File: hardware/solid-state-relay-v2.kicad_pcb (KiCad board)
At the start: 2 copper layers, 40 x 19 mm, 22 parts, among them P1 CON-SENSOR2, P2 TST, P3 TST, P5 BOOT, Q1 2N7002P, U1 XMC110024, U2 DRILL, U3 DRILL

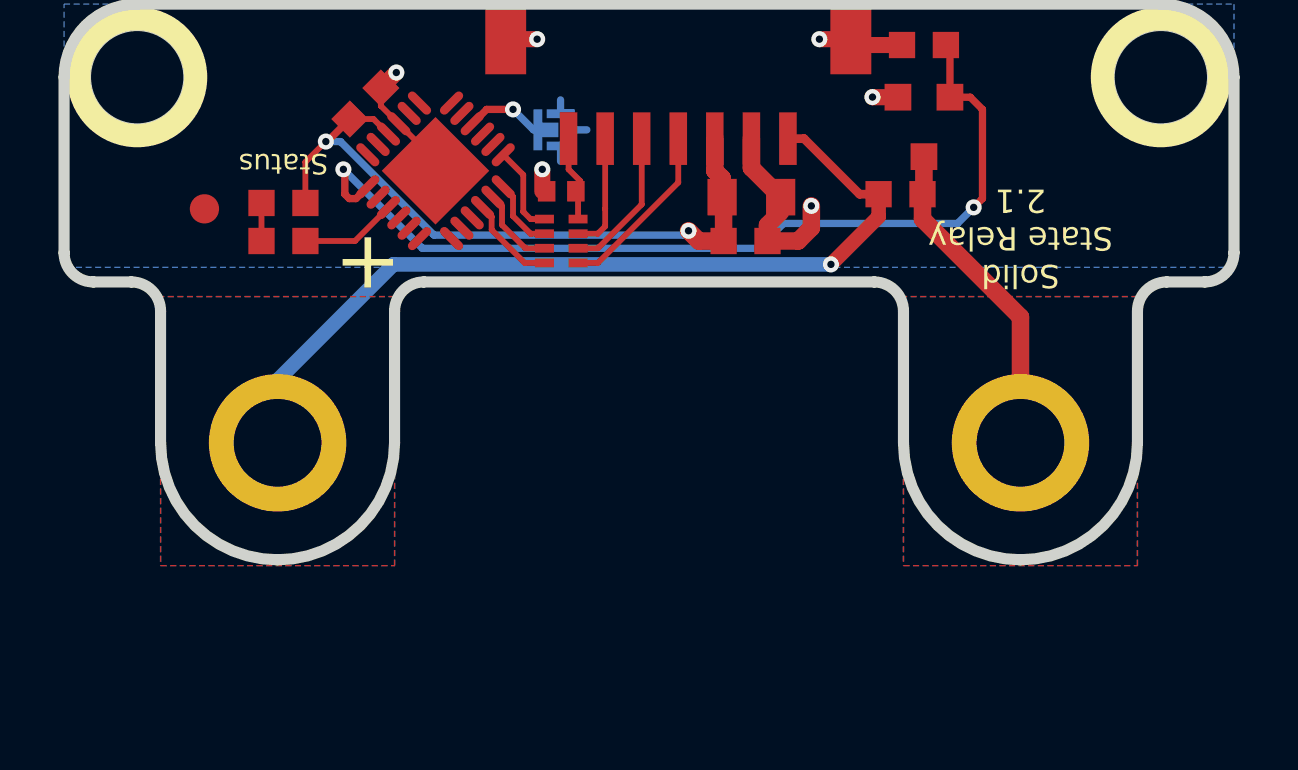
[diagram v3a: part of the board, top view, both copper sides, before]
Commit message: version 2.2: add slotted holes
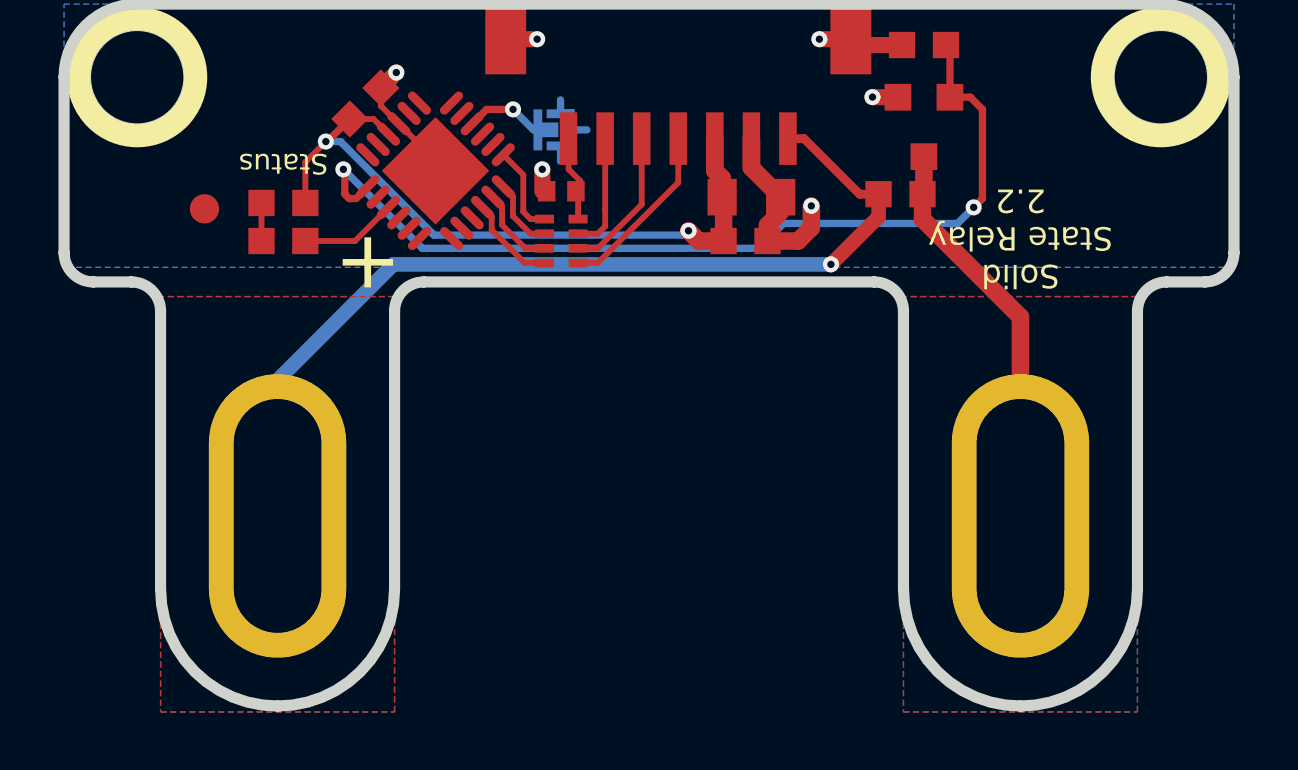
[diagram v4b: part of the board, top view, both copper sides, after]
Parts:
- moved P2 2.50 mm to (137.8, 105.1), turned to 0 degrees
- moved P3 2.50 mm to (163.2, 105.1), turned to 0 degrees
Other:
- board size 40 x 19 mm -> 40 x 24 mm
- board text added: "Copyright Tinkerforge GmbH 2025. This documentation describes Open Hardware and is licensed under the CERN OHL v. 1.1. You may redistribute and modify this documentation under the terms of the CERN OHL v.1.1. (http://ohwr.org/cernohl). This documentation is distributed WITHOUT ANY EXPRESS OR IMPLIED WARRANTY, INCLUDING OF MERCHANTABILITY, SATISFACTORY QUALITY AND FITNESS FOR A PARTICULAR PURPOSE.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"
- board text added: "Solid State Relay 2.2"
- board text removed: "Copyright Tinkerforge GmbH 2023. This documentation describes Open Hardware and is licensed under the CERN OHL v. 1.1. You may redistribute and modify this documentation under the terms of the CERN OHL v.1.1. (http://ohwr.org/cernohl). This documentation is distributed WITHOUT ANY EXPRESS OR IMPLIED WARRANTY, INCLUDING OF MERCHANTABILITY, SATISFACTORY QUALITY AND FITNESS FOR A PARTICULAR PURPOSE.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"
- board text removed: "Solid State Relay 2.1"

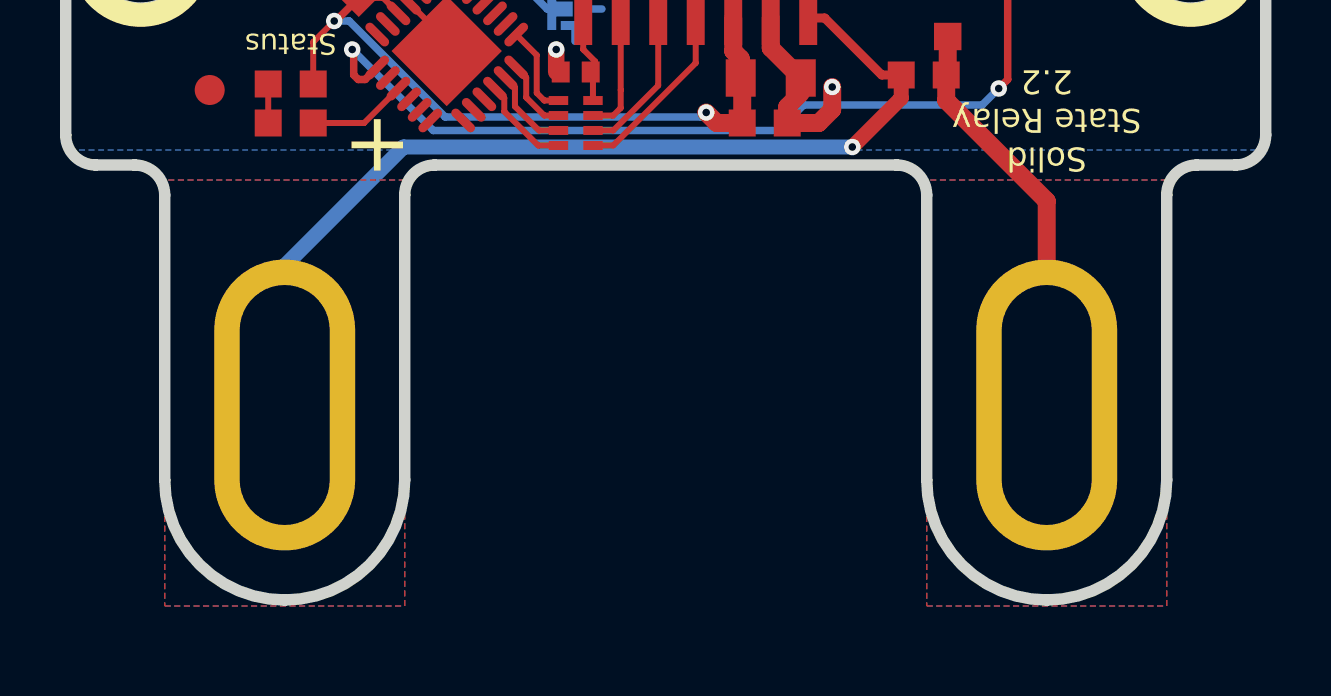
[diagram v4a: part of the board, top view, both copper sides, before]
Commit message: adapt outline to 5mm grid
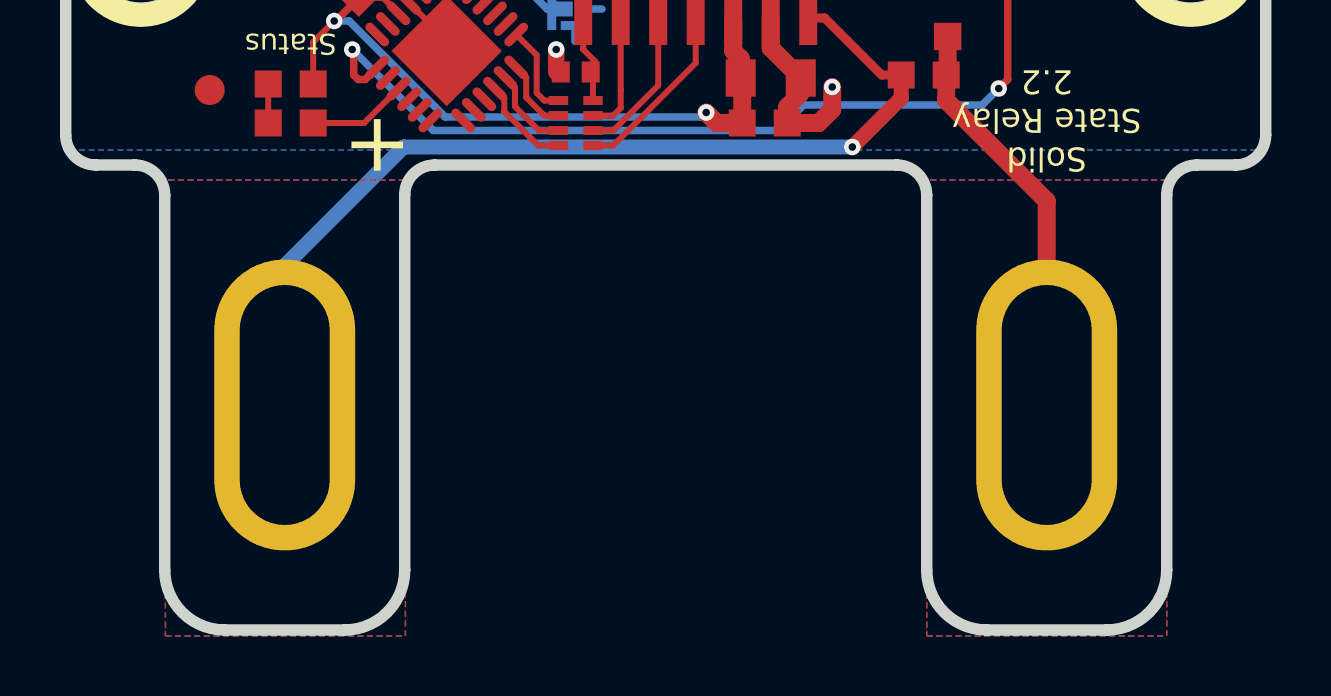
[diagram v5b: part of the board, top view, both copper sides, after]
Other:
- board size 40 x 24 mm -> 40 x 25 mm

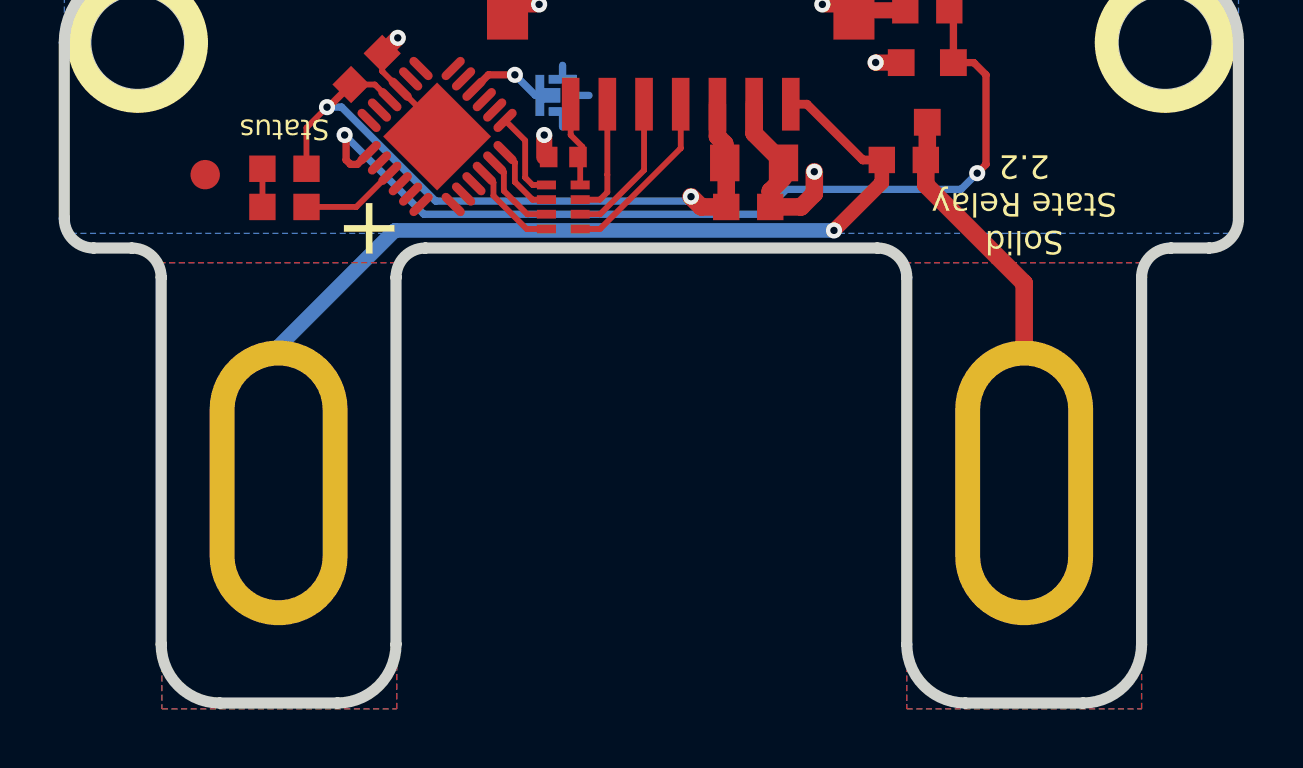
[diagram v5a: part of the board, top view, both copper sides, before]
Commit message: small dimensions changes
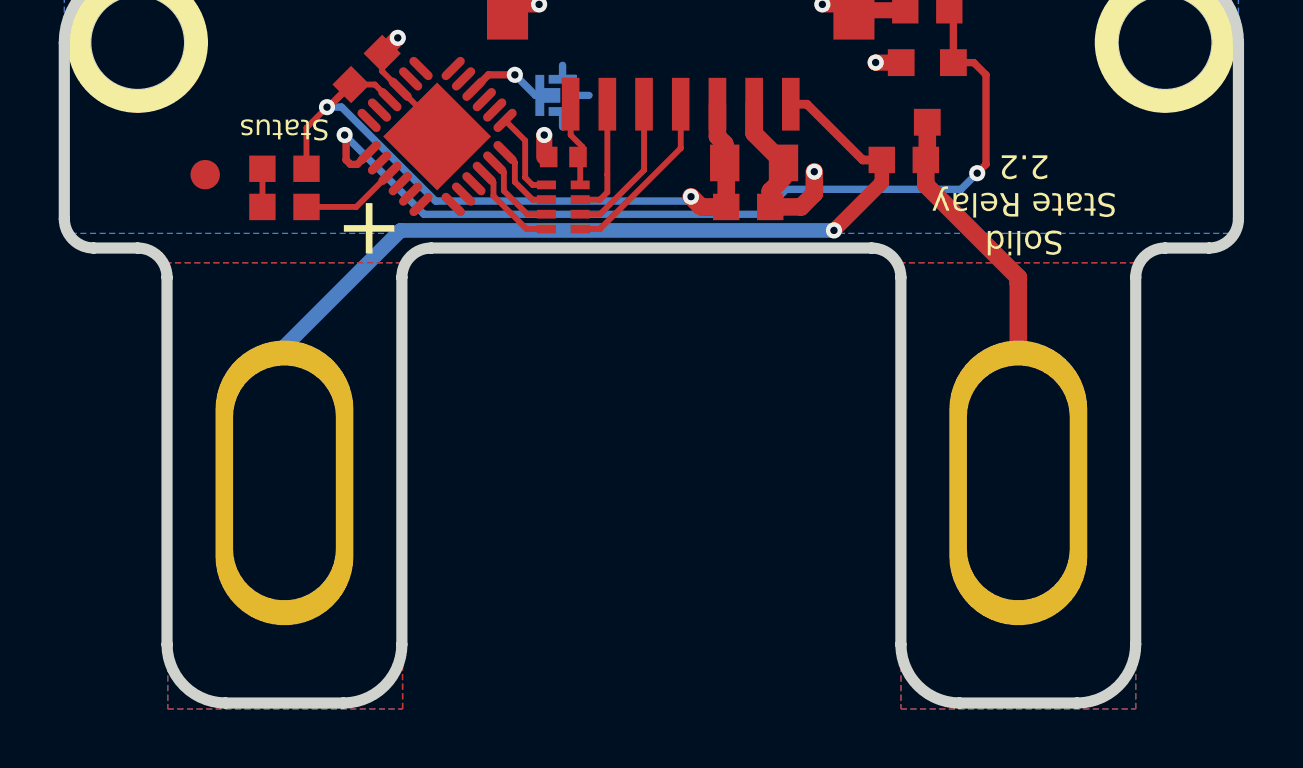
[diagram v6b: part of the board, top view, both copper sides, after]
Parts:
- moved P2 0.20 mm to (138.0, 105.1)
- moved P3 0.20 mm to (163.0, 105.1)
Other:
- outline, holes or cut-outs redrawn
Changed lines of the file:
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@@
 	(footprint "kicad-libraries:Drill"
 		(layer "F.Cu")
-		(at 163.2 105.1)
+		(at 163 105.1)
 		(property "Reference" "P3"
 			(at 0 0 0)
@@
 			(at 0 0)
 			(size 4.7 9.7)
-			(drill oval 3 8)
+			(drill oval 3.5 8)
 			(layers "*.Cu" "*.Mask")
 			(remove_unused_layers no)
@@
 	(footprint "kicad-libraries:Drill"
 		(layer "F.Cu")
-		(at 137.8 105.1)
+		(at 138 105.1)
 		(property "Reference" "P2"
 			(at 0 0 0)
@@
 			(at 0 0)
 			(size 4.7 9.7)
-			(drill oval 3 8)
+			(drill oval 3.5 8)
 			(layers "*.Cu" "*.Mask")
 			(remove_unused_layers no)
@@
 	)
 	(gr_line
-		(start 168.2 97.1)
+		(start 168 97.1)
 		(end 169.5 97.1)
 		(stroke
@@
 	)
 	(gr_arc
-		(start 167.2 98.1)
-		(mid 167.492893 97.392893)
-		(end 168.2 97.1)
+		(start 167 98.1)
+		(mid 167.292893 97.392893)
+		(end 168 97.1)
 		(stroke
 			(width 0.381)
@@
 	)
 	(gr_line
-		(start 133.8 110.6)
-		(end 133.8 98.1)
+		(start 134 110.6)
+		(end 134 98.1)
 		(stroke
 			(width 0.381)
@@
 	)
 	(gr_line
-		(start 161.2 112.6)
-		(end 165.2 112.6)
+		(start 161 112.6)
+		(end 165 112.6)
 		(stroke
 			(width 0.381)
@@
 	)
 	(gr_arc
-		(start 132.8 97.1)
-		(mid 133.507107 97.392893)
-		(end 133.8 98.1)
+		(start 133 97.1)
+		(mid 133.707107 97.392893)
+		(end 134 98.1)
 		(stroke
 			(width 0.381)
@@
 	)
 	(gr_arc
-		(start 141.8 110.6)
-		(mid 141.214214 112.014214)
-		(end 139.8 112.6)
+		(start 142 110.6)
+		(mid 141.414214 112.014214)
+		(end 140 112.6)
 		(stroke
 			(width 0.381)
@@
 	)
 	(gr_line
-		(start 135.8 112.6)
-		(end 139.8 112.6)
+		(start 136 112.6)
+		(end 140 112.6)
 		(stroke
 			(width 0.381)
@@
 	)
 	(gr_arc
-		(start 161.2 112.6)
-		(mid 159.785786 112.014214)
-		(end 159.2 110.6)
+		(start 161 112.6)
+		(mid 159.585786 112.014214)
+		(end 159 110.6)
 		(stroke
 			(width 0.381)
@@
 	)
 	(gr_arc
-		(start 158.2 97.1)
-		(mid 158.907107 97.392893)
-		(end 159.2 98.1)
+		(start 158 97.1)
+		(mid 158.707107 97.392893)
+		(end 159 98.1)
 		(stroke
 			(width 0.381)
@@
 	(gr_line
 		(start 131.5 97.1)
-		(end 132.8 97.1)
+		(end 133 97.1)
 		(stroke
 			(width 0.381)
@@
 	)
 	(gr_line
-		(start 158.2 97.1)
-		(end 142.8 97.1)
+		(start 158 97.1)
+		(end 143 97.1)
 		(stroke
 			(width 0.381)
@@
 	)
 	(gr_arc
-		(start 135.8 112.6)
-		(mid 134.385786 112.014214)
-		(end 133.8 110.6)
+		(start 136 112.6)
+		(mid 134.585786 112.014214)
+		(end 134 110.6)
 		(stroke
 			(width 0.381)
@@
 	)
 	(gr_line
-		(start 141.8 110.6)
-		(end 141.8 98.1)
+		(start 142 110.6)
+		(end 142 98.1)
 		(stroke
 			(width 0.381)
@@
 	)
 	(gr_arc
-		(start 167.2 110.6)
-		(mid 166.614214 112.014214)
-		(end 165.2 112.6)
+		(start 167 110.6)
+		(mid 166.414214 112.014214)
+		(end 165 112.6)
 		(stroke
 			(width 0.381)
@@
 	)
 	(gr_arc
-		(start 141.8 98.1)
-		(mid 142.092893 97.392893)
-		(end 142.8 97.1)
+		(start 142 98.1)
+		(mid 142.292893 97.392893)
+		(end 143 97.1)
 		(stroke
 			(width 0.381)
@@
 	)
 	(gr_line
-		(start 159.2 110.6)
-		(end 159.2 98.1)
+		(start 159 110.6)
+		(end 159 98.1)
 		(stroke
 			(width 0.381)
@@
 	)
 	(gr_line
-		(start 167.2 110.6)
-		(end 167.2 98.1)
+		(start 167 110.6)
+		(end 167 98.1)
 		(stroke
 			(width 0.381)
@@
 	)
 	(segment
-		(start 137.8 100.46)
-		(end 137.8 102.6)
+		(start 138 100.46)
+		(end 138 102.6)
 		(width 0.5)
 		(layer "B.Cu")
@@
 	(segment
 		(start 156.72 96.5)
-		(end 141.76 96.5)
+		(end 141.96 96.5)
 		(width 0.5)
 		(layer "B.Cu")
@@
 	)
 	(segment
-		(start 141.76 96.5)
-		(end 137.8 100.46)
+		(start 141.96 96.5)
+		(end 138 100.46)
 		(width 0.5)
 		(layer "B.Cu")
@@
 	)
 	(segment
-		(start 159.85 94.95)
-		(end 163.2 98.3)
+		(start 163 98.3)
+		(end 163 102.6)
 		(width 0.59944)
 		(layer "F.Cu")
@@
 	)
 	(segment
-		(start 163.2 98.3)
-		(end 163.2 102.6)
+		(start 159.9 92.816)
+		(end 159.9 94.05)
 		(width 0.59944)
 		(layer "F.Cu")
@@
 	)
 	(segment
-		(start 159.9 92.816)
-		(end 159.9 94.05)
+		(start 163 98.1)
+		(end 163 98.3)
+		(width 0.59944)
+		(layer "F.Cu")
+		(net 31)
+	)
+	(segment
+		(start 159.85 94.95)
+		(end 163 98.1)
 		(width 0.59944)
 		(layer "F.Cu")
@@
 		(polygon
 			(pts
-				(xy 141.8 97.6) (xy 133.8 97.6) (xy 133.825 112.8) (xy 141.825 112.8)
+				(xy 142 97.6) (xy 134 97.6) (xy 134.025 112.8) (xy 142.025 112.8)
 			)
 		)
@@
 		(polygon
 			(pts
-				(xy 167.2 112.8) (xy 167.2 97.6) (xy 159.2 97.6) (xy 159.2 112.8)
+				(xy 167 112.8) (xy 167 97.6) (xy 159 97.6) (xy 159 112.8)
 			)
 		)
@@
 		(polygon
 			(pts
-				(xy 141.825 112.8) (xy 141.8 97.6) (xy 133.8 97.6) (xy 133.825 112.8)
+				(xy 142.025 112.8) (xy 142 97.6) (xy 134 97.6) (xy 134.025 112.8)
 			)
 		)
@@
 		(polygon
 			(pts
-				(xy 159.2 97.6) (xy 159.2 112.8) (xy 167.2 112.8) (xy 167.2 97.6)
+				(xy 159 97.6) (xy 159 112.8) (xy 167 112.8) (xy 167 97.6)
 			)
 		)
